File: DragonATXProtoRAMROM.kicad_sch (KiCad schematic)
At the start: 29 parts, among them IC1 28C256, IC10 74LS244, IC11 74LS08, IC2 MK4164N, IC3 MK4164N, IC4 MK4164N, IC5 MK4164N, IC6 MK4164N, IC7 MK4164N, IC8 MK4164N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

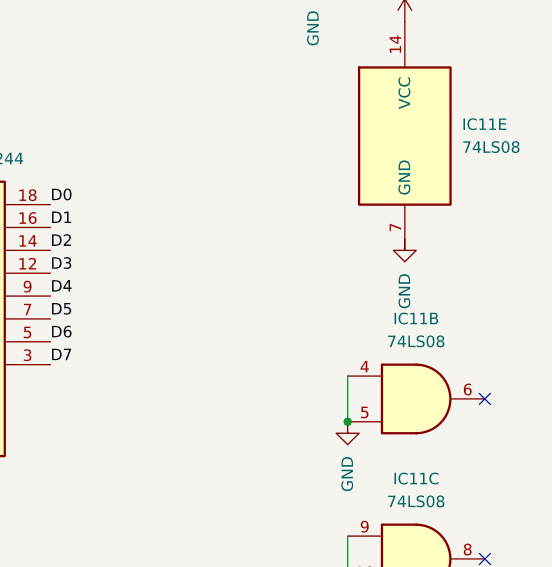
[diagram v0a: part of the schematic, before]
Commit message: fix missing gnd pin connection
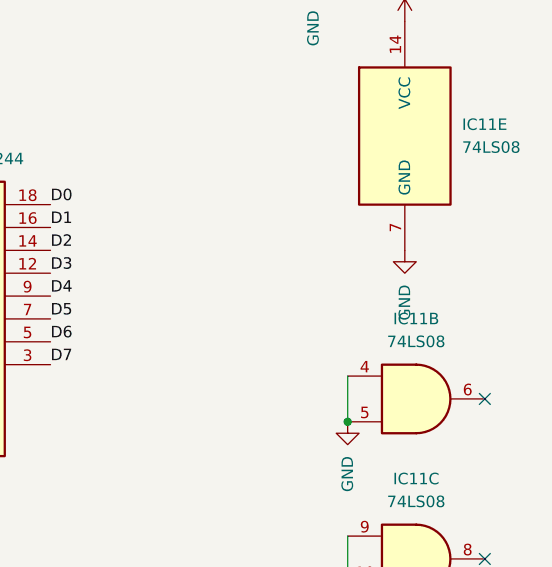
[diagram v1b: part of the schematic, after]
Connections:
- net GND: now also IC11.7 (GND)
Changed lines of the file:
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@@
 			)
 		)
-		(property "Description" ""
+		(property "Description" "Power symbol creates a global label with name \"GND\" , ground"
 			(at 165.1 173.99 0)
 			(effects
@@
 	(symbol
 		(lib_id "power:GND")
-		(at 267.97 104.14 0)
+		(at 267.97 105.41 0)
 		(mirror y)
 		(unit 1)
@@
 		(dnp no)
 		(property "Reference" "#PWR018"
-			(at 267.97 110.49 0)
+			(at 267.97 111.76 0)
 			(effects
 				(font
@@
 		)
 		(property "Value" "GND"
-			(at 267.9701 107.95 90)
+			(at 267.9701 109.22 90)
 			(effects
 				(font
@@
 		)
 		(property "Footprint" ""
-			(at 267.97 104.14 0)
+			(at 267.97 105.41 0)
 			(effects
 				(font
@@
 		)
 		(property "Datasheet" ""
-			(at 267.97 104.14 0)
+			(at 267.97 105.41 0)
 			(effects
 				(font
@@
 		)
 		(property "Description" "Power symbol creates a global label with name \"GND\" , ground"
-			(at 267.97 104.14 0)
-			(effects
-				(font
+			(at 267.97 105.41 0)
+			(effects
+				(font
